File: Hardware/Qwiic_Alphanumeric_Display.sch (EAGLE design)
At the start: 32 parts, among them J4 Vertical Qwiic Connector, J5 Vertical Qwiic Connector

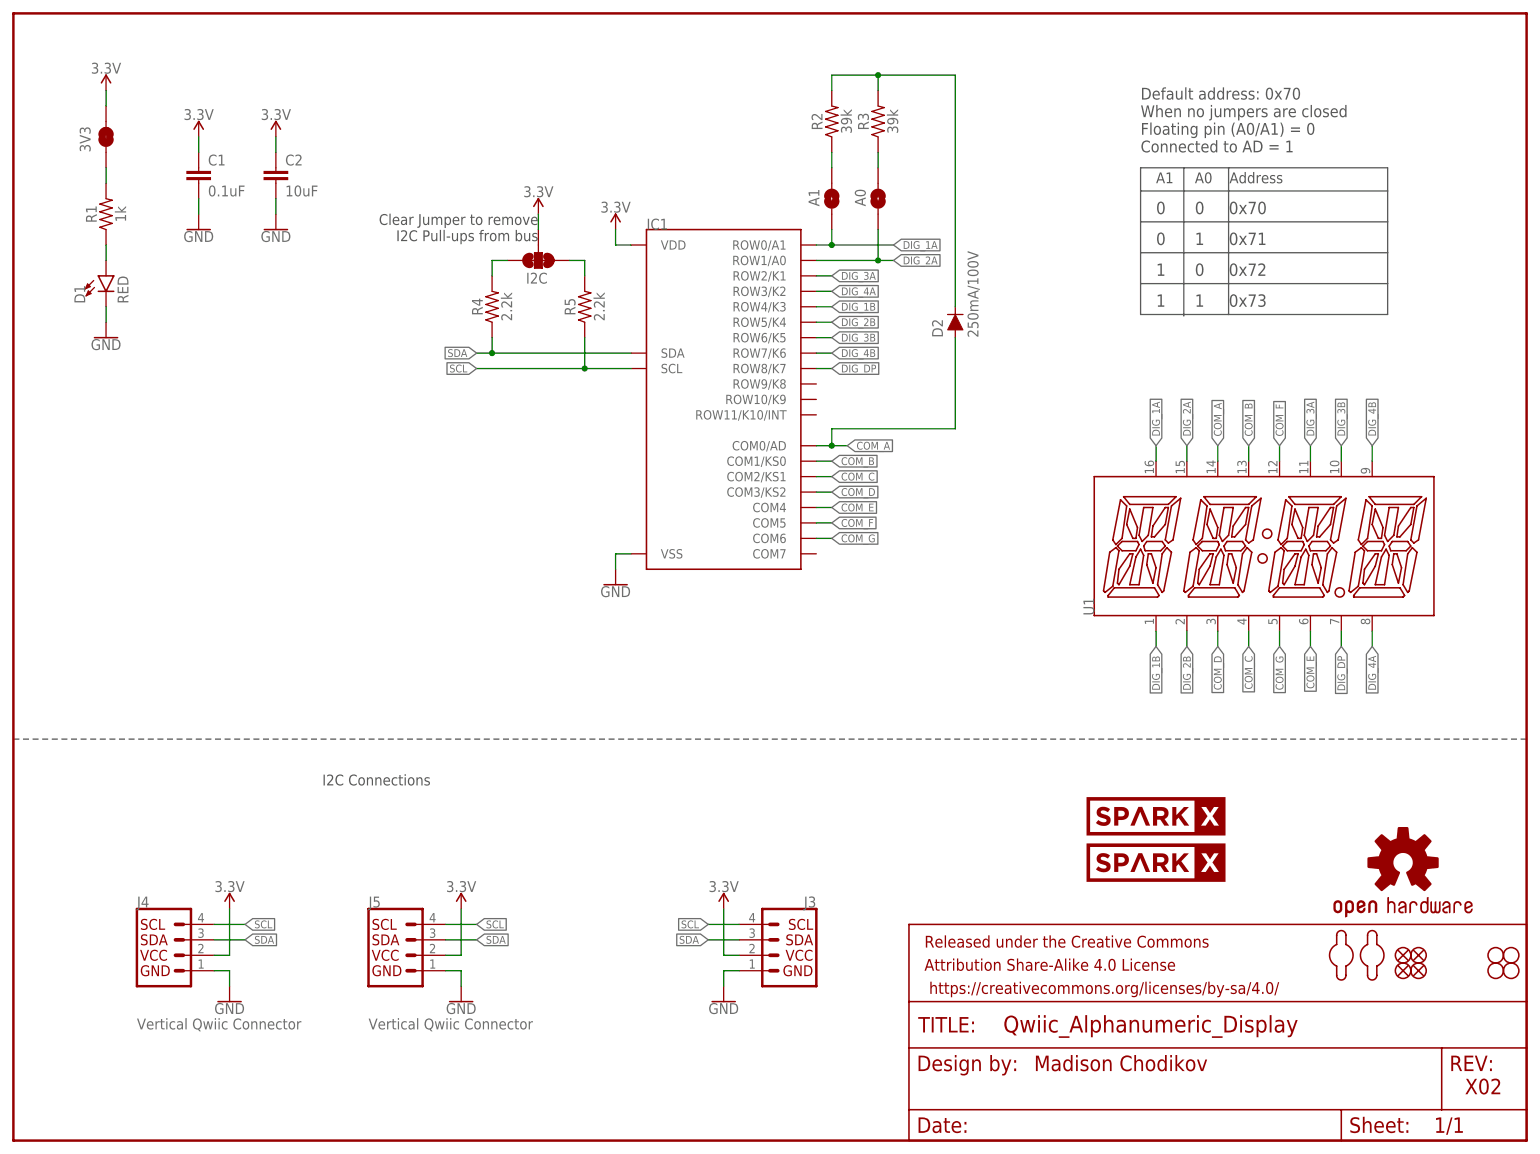
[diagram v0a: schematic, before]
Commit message: Update design for protos
Add 5V boost circuit for ht16k33
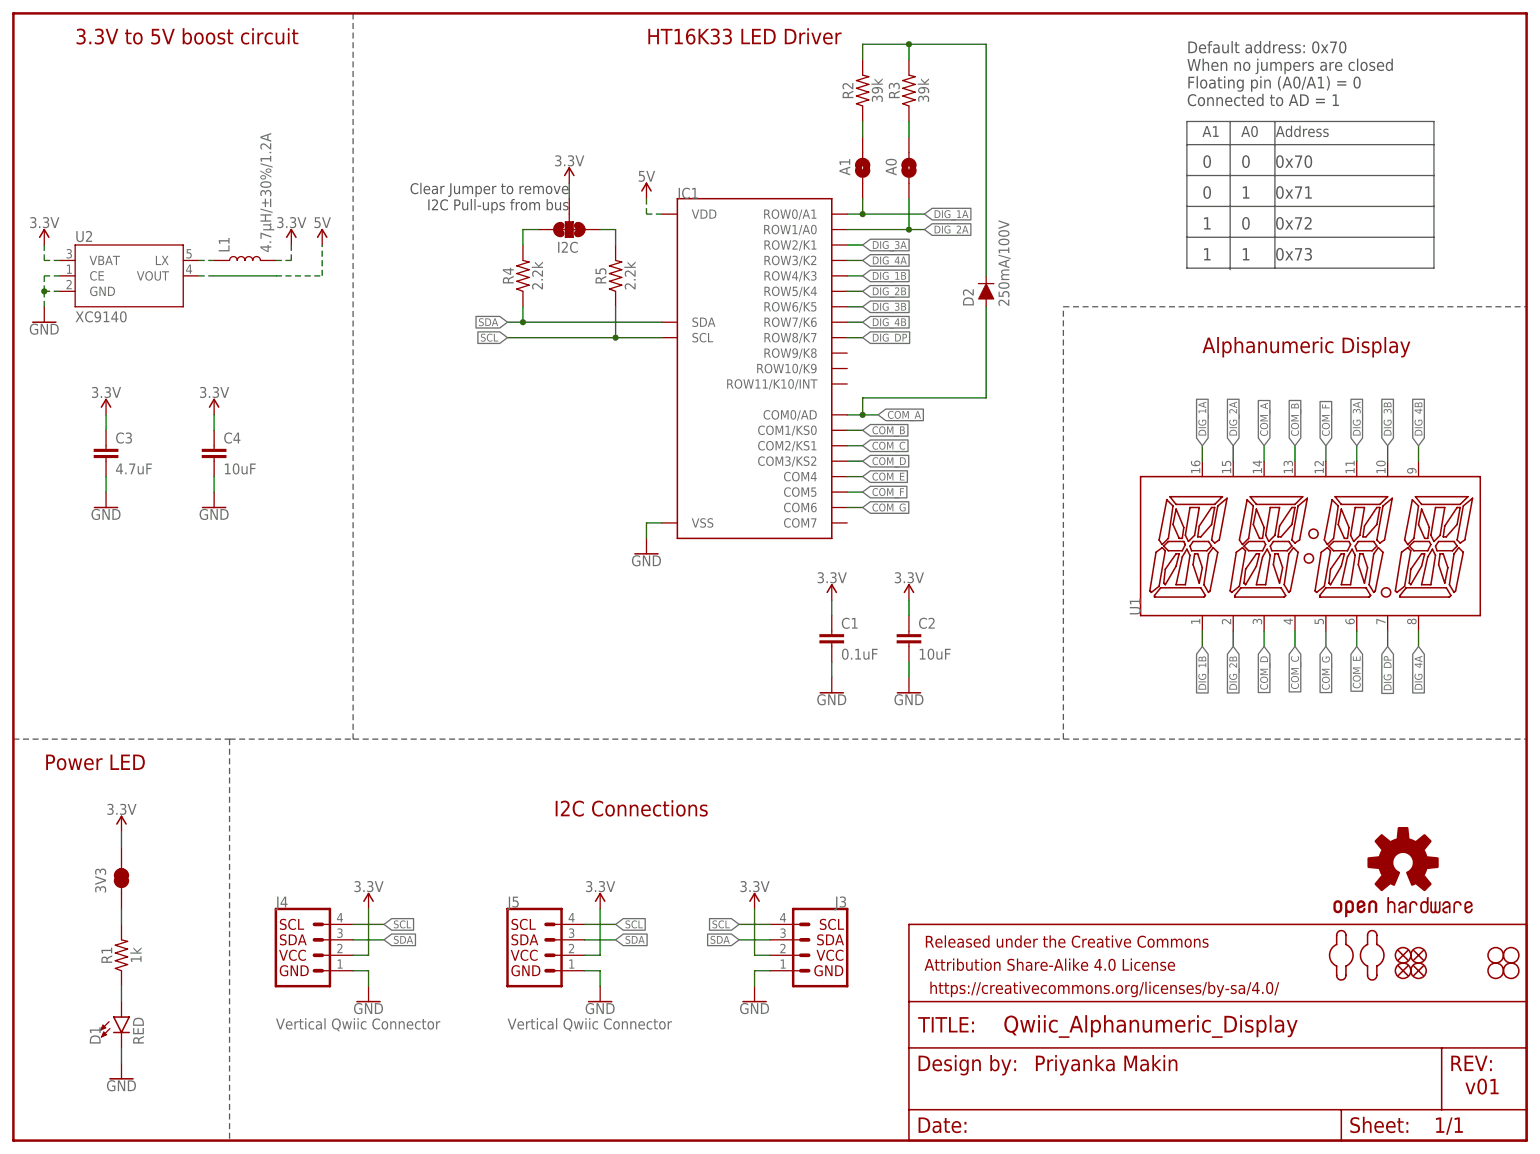
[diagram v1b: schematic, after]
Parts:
- removed U$7, U$8: SPARKX-LOGO4, SparkX:SPARKX-LOGO4
- added C3: 4.7uF, SparkFun-Capacitors:4.7UF-0603-6.3V-(10%)
- added C4: 10uF, SparkFun-Capacitors:10UF-0603-6.3V-20%
- added L1: 4.7µH/±30%/1.2A, SparkFun-Coils:INDUCTOR-CDRH-4.7UH
- added U2: XC9140, SparkFun-IC-Power:XC9140
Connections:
- new net 5V: IC1.VDD
- new net N$10: L1.1, U2.LX
- new net N$11: U2.VOUT
- net 3.3V: now also C3.1, C4.1, L1.2, U2.VBAT; no longer IC1.VDD
- net GND: now also C3.2, C4.2, U2.CE, U2.GND
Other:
- note added: "3.3V to 5V boost circuit"
- note added: "Alphanumeric Display"
- note added: "HT16K33 LED Driver"
- note added: "Power LED"
- note added: "Priyanka Makin"
- note added: "v01"
- note removed: "Madison Chodikov"
- note removed: "X02"
- moved on the sheet: 3V3, A0, A1, C1, C2, D1, D2, I2C, IC1, J3, J4, J5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

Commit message: Run schematic/board autochecklist
Update font to vector
Make sure all parts (except for new ones) are in SF Eagle libs
Add measures
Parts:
- added LOGO2, LOGO3: SFE_LOGO_NAME.1_INCH, SparkFun-Aesthetics:SFE_LOGO_NAME.1_INCH
- added LOGO4: SFE_LOGO_FLAME.1_INCH, SparkFun-Aesthetics:SFE_LOGO_FLAME.1_INCH
- L1: value 4.7µH/±30%/1.2A -> 4.7µH
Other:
- note added: "Cut jumper to remove 3.3V LED."
- note added: "Cut jumper to remove I2C Pull-ups from bus"
- note removed: "Clear Jumper to remove I2C Pull-ups from bus"
- moved on the sheet: 3V3, D1, R1

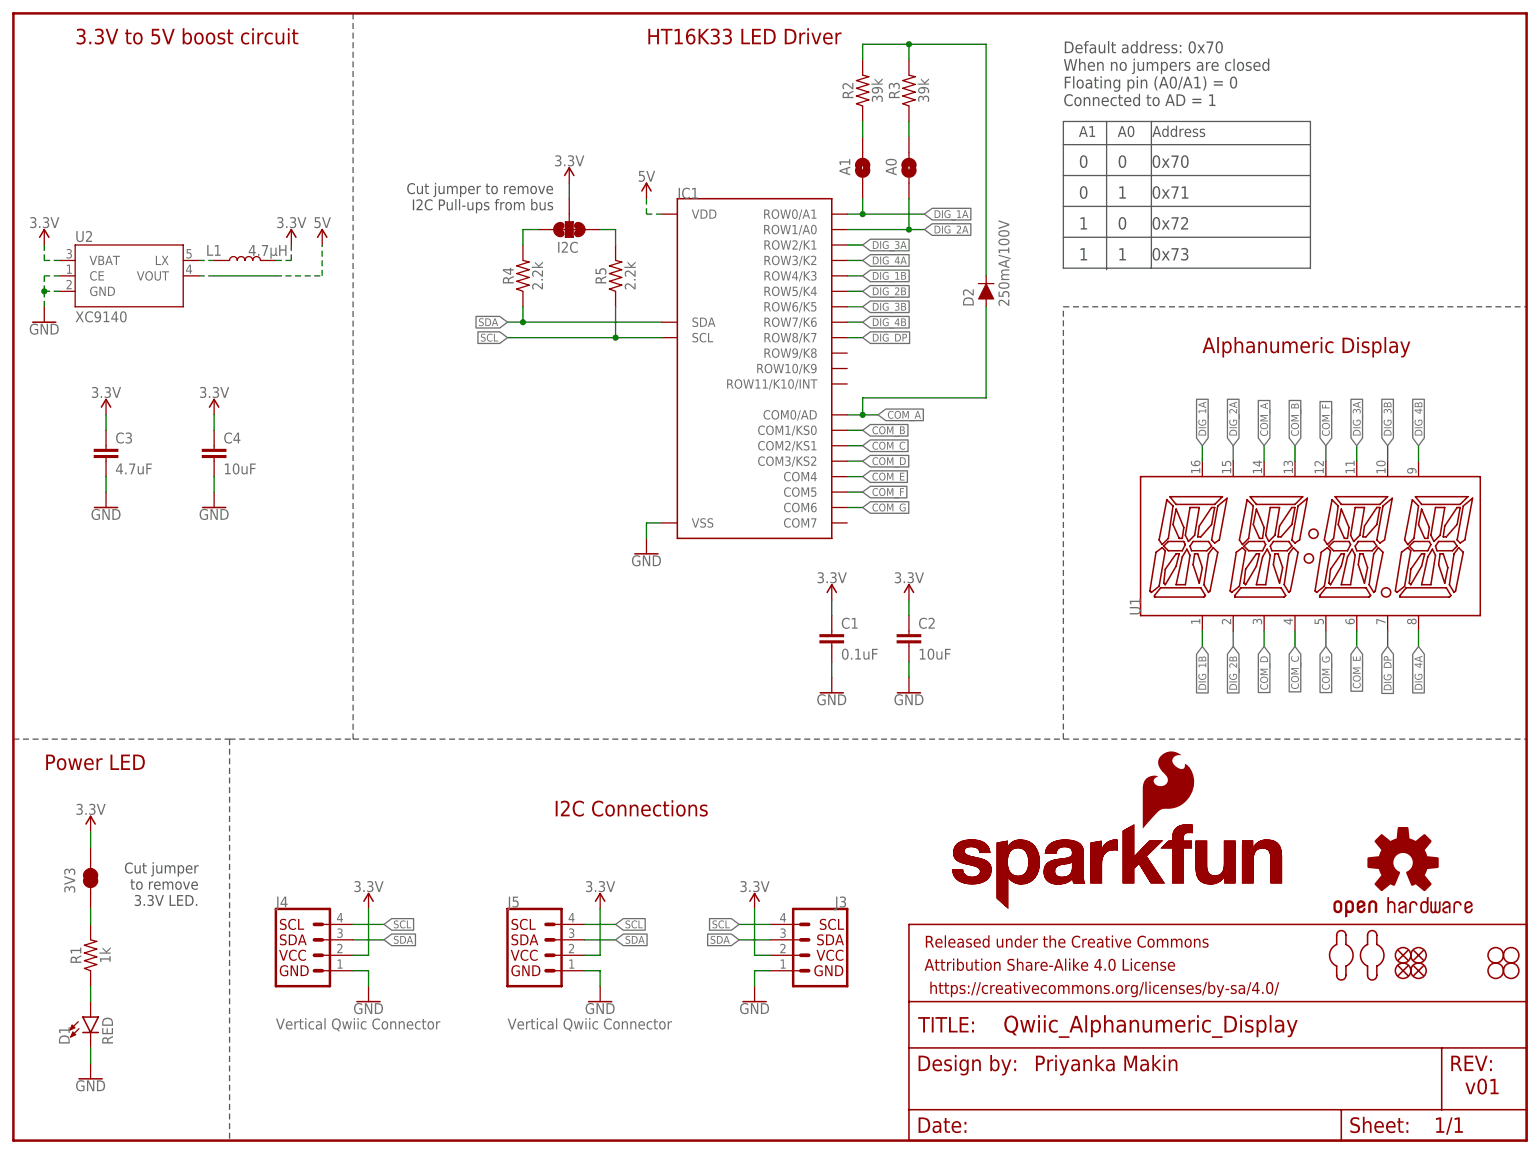
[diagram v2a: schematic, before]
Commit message: Updates after proto review
Update HT16K33 to VK16K33
Compared datasheets, it’s a drop in replacement!
Removed PWR LED and jumper
5V net now connects to the LED driver IC
New mounting hole design
I2C pullups became 4.7k and removed jumper
You can only connect up to 4 displays on one bus
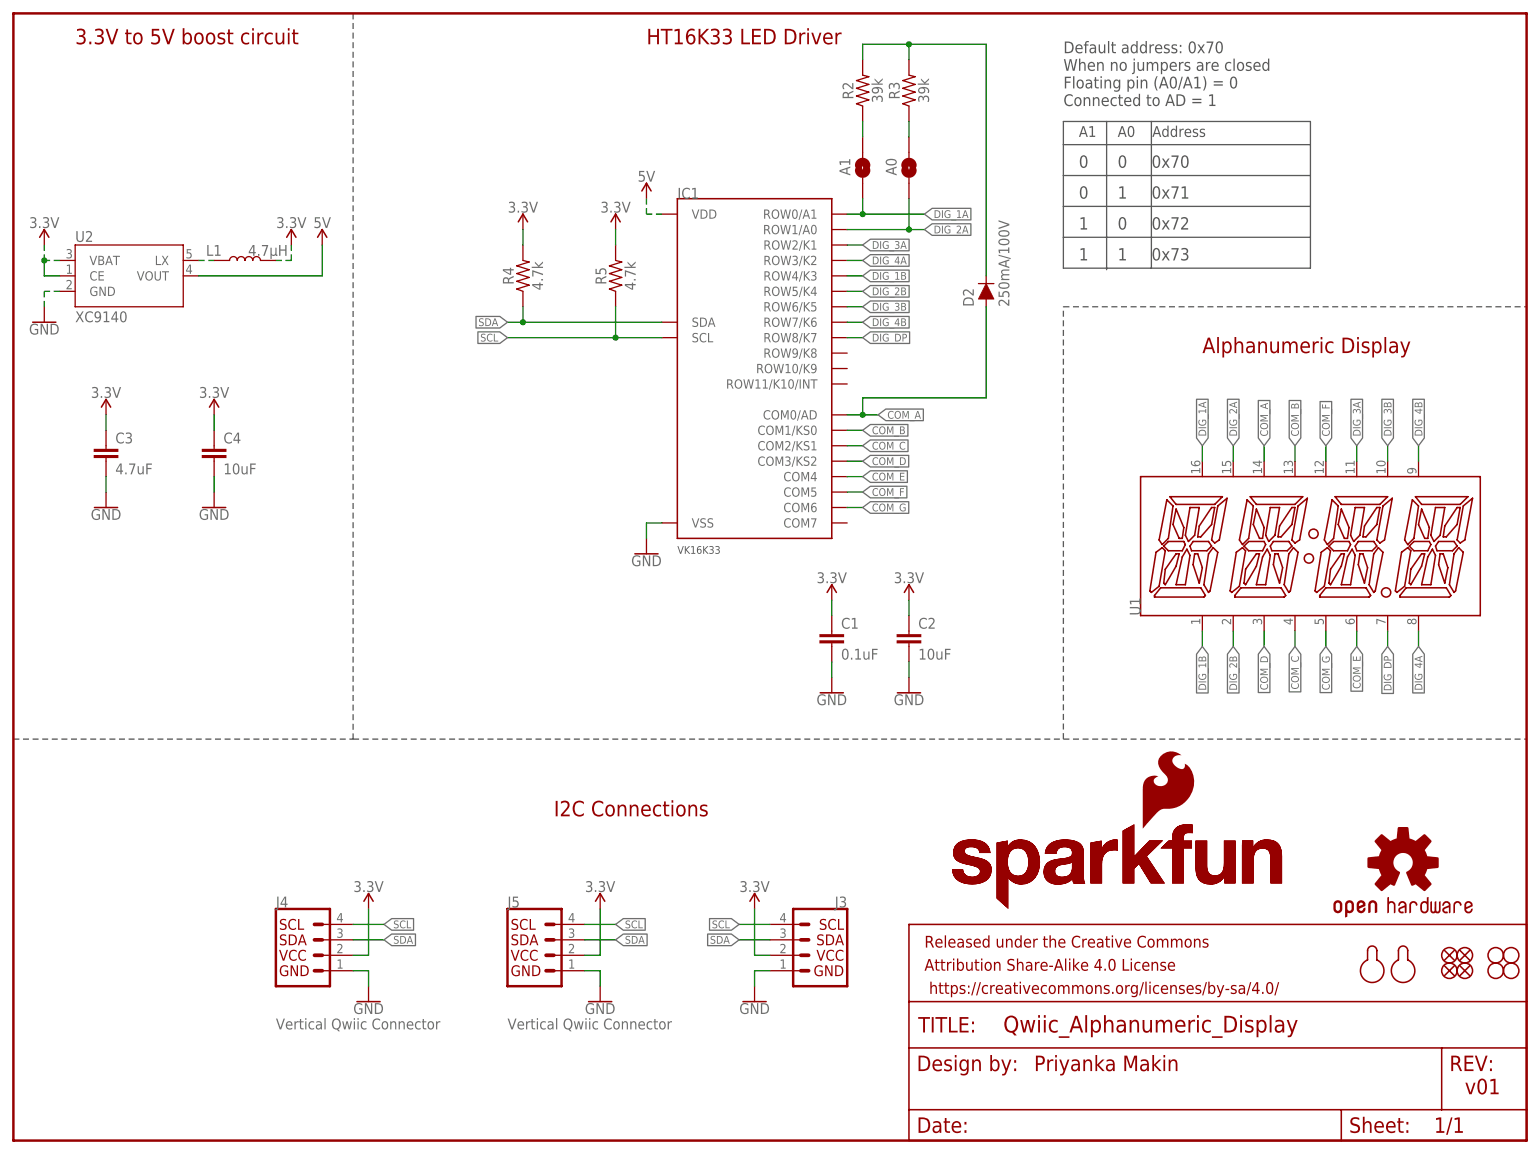
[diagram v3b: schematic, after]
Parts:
- removed 3V3: JUMPER-SMT_2_NC_TRACE_SILK, SparkFun-Jumpers:JUMPER-SMT_2_NC_TRACE_SILK
- removed D1: RED, SparkFun-LED:LED-RED0603
- removed I2C: JUMPER-SMT_3_2-NC_TRACE_SILK, SparkFun-Jumpers:JUMPER-SMT_3_2-NC_TRACE_SILK
- removed R1: 1k, SparkFun-Resistors:1KOHM-0603-1/10W-1%
- removed U$18, U$19: MOUNTING_HOLE_M2-0.4X6, Alphanumeric_Display_Library:MOUNTING_HOLE_M2-0.4X6
- added U$3, U$7: MOUNTING_HOLE_M2-0.4X6, Alphanumeric_Display_Library:MOUNTING_HOLE_M2-0.4X6
- IC1: device Alphanumeric_Display_Library:HT16K33 -> Alphanumeric_Display_Library:VK16K33VK16K33; PROD_ID IC-14891 -> (none)
- R4, R5: value 2.2k -> 4.7k; device SparkFun-Resistors:2.2KOHM-0603-1/10W-1% -> SparkFun-Resistors:4.7KOHM-0603-1/10W-1%
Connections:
- removed net N$1: D1.A, R1.1
- removed net N$11: U2.VOUT
- removed net N$4: I2C.1, R5.2
- removed net N$5: I2C.3, R4.2
- removed net N$7: 3V3.1, R1.2
- net 3.3V: now also R4.2, R5.2, U2.CE; no longer 3V3.2, I2C.2
- net 5V: now also U2.VOUT
- net GND: no longer D1.C, U2.CE
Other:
- note added: "VK16K33"
- note removed: "Cut jumper to remove 3.3V LED."
- note removed: "Cut jumper to remove I2C Pull-ups from bus"
- note removed: "Power LED"
